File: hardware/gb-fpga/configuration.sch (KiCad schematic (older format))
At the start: 13 parts, among them U1 xc7s25ftgb196, U2 MX25R3235FZBxx1

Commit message: Switch from 0603 to 0402 footprints
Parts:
- C1: footprint Capacitor_SMD:C_0603_1608Metric -> Capacitor_SMD:C_0402_1005Metric
- D1: footprint LED_SMD:LED_0603_1608Metric -> LED_SMD:LED_0402_1005Metric
- R1, R2, R3, R4, R5, R6, R7, R8, R9: footprint Resistor_SMD:R_0603_1608Metric -> Resistor_SMD:R_0402_1005Metric
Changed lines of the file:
@@
 F 0 "C1" H 9692 3746 50  0000 L CNN
 F 1 "100nF" H 9692 3655 50  0000 L CNN
-F 2 "Capacitor_SMD:C_0603_1608Metric" H 9600 3700 50  0001 C CNN
+F 2 "Capacitor_SMD:C_0402_1005Metric" H 9600 3700 50  0001 C CNN
 F 3 "~" H 9600 3700 50  0001 C CNN
 	1    9600 3700
@@
 F 0 "R1" H 7400 3400 50  0000 C CNN
 F 1 "4.7k" H 7400 3500 50  0000 C CNN
-F 2 "Resistor_SMD:R_0603_1608Metric" H 7550 3450 50  0001 C CNN
+F 2 "Resistor_SMD:R_0402_1005Metric" H 7550 3450 50  0001 C CNN
 F 3 "~" H 7550 3450 50  0001 C CNN
 	1    7550 3450
@@
 F 0 "R3" H 7050 3400 50  0000 C CNN
 F 1 "1.8k" H 7050 3500 50  0000 C CNN
-F 2 "Resistor_SMD:R_0603_1608Metric" H 7200 3450 50  0001 C CNN
+F 2 "Resistor_SMD:R_0402_1005Metric" H 7200 3450 50  0001 C CNN
 F 3 "~" H 7200 3450 50  0001 C CNN
 	1    7200 3450
@@
 F 0 "R2" H 6700 3400 50  0000 C CNN
 F 1 "1.8k" H 6700 3500 50  0000 C CNN
-F 2 "Resistor_SMD:R_0603_1608Metric" H 6850 3450 50  0001 C CNN
+F 2 "Resistor_SMD:R_0402_1005Metric" H 6850 3450 50  0001 C CNN
 F 3 "~" H 6850 3450 50  0001 C CNN
 	1    6850 3450
@@
 F 0 "R7" H 2150 3150 50  0000 C CNN
 F 1 "4.7k" H 2150 3250 50  0000 C CNN
-F 2 "Resistor_SMD:R_0603_1608Metric" H 2300 3200 50  0001 C CNN
+F 2 "Resistor_SMD:R_0402_1005Metric" H 2300 3200 50  0001 C CNN
 F 3 "~" H 2300 3200 50  0001 C CNN
 	1    2300 3200
@@
 F 0 "R6" H 1850 3150 50  0000 C CNN
 F 1 "4.7k" H 1850 3250 50  0000 C CNN
-F 2 "Resistor_SMD:R_0603_1608Metric" H 2000 3200 50  0001 C CNN
+F 2 "Resistor_SMD:R_0402_1005Metric" H 2000 3200 50  0001 C CNN
 F 3 "~" H 2000 3200 50  0001 C CNN
 	1    2000 3200
@@
 F 0 "R5" H 1550 3150 50  0000 C CNN
 F 1 "4.7k" H 1550 3250 50  0000 C CNN
-F 2 "Resistor_SMD:R_0603_1608Metric" H 1700 3200 50  0001 C CNN
+F 2 "Resistor_SMD:R_0402_1005Metric" H 1700 3200 50  0001 C CNN
 F 3 "~" H 1700 3200 50  0001 C CNN
 	1    1700 3200
@@
 F 0 "R8" H 2650 3050 50  0000 C CNN
 F 1 "200" H 2650 3150 50  0000 C CNN
-F 2 "Resistor_SMD:R_0603_1608Metric" H 2800 3100 50  0001 C CNN
+F 2 "Resistor_SMD:R_0402_1005Metric" H 2800 3100 50  0001 C CNN
 F 3 "~" H 2800 3100 50  0001 C CNN
 	1    2800 3100
@@
 F 0 "D1" V 2196 4730 50  0000 R CNN
 F 1 "LED" V 2105 4730 50  0000 R CNN
-F 2 "LED_SMD:LED_0603_1608Metric" V 2150 4800 50  0001 C CNN
+F 2 "LED_SMD:LED_0402_1005Metric" V 2150 4800 50  0001 C CNN
 F 3 "~" V 2150 4800 50  0001 C CNN
 	1    2150 4800
@@
 F 0 "R9" H 2000 4400 50  0000 C CNN
 F 1 "100" H 2000 4500 50  0000 C CNN
-F 2 "Resistor_SMD:R_0603_1608Metric" H 2150 4450 50  0001 C CNN
+F 2 "Resistor_SMD:R_0402_1005Metric" H 2150 4450 50  0001 C CNN
 F 3 "~" H 2150 4450 50  0001 C CNN
 	1    2150 4450
@@
 F 0 "R4" H 5550 3050 50  0000 C CNN
 F 1 "1k" H 5550 3150 50  0000 C CNN
-F 2 "Resistor_SMD:R_0603_1608Metric" H 5700 3100 50  0001 C CNN
+F 2 "Resistor_SMD:R_0402_1005Metric" H 5700 3100 50  0001 C CNN
 F 3 "~" H 5700 3100 50  0001 C CNN
 	1    5700 3100

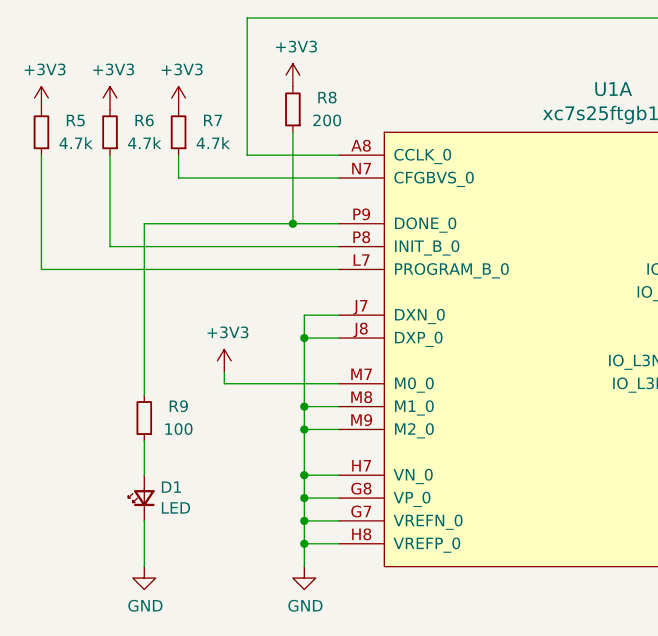
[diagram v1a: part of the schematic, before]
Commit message: Add chargeing indicator LED
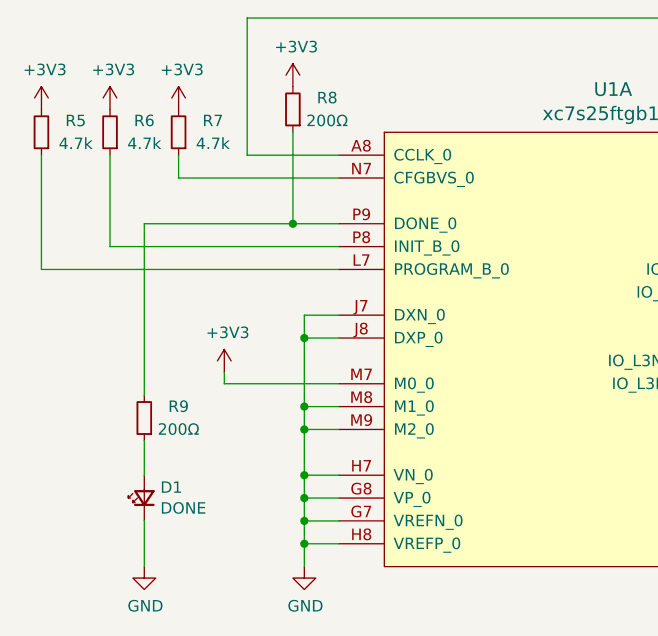
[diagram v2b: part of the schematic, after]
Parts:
- D1: value LED -> DONE
- R8: value 200 -> 200Ω
- R9: value 100 -> 200Ω
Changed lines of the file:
@@
 P 2800 3100
 F 0 "R8" H 2650 3050 50  0000 C CNN
-F 1 "200" H 2650 3150 50  0000 C CNN
+F 1 "200Ω" H 2650 3150 50  0000 C CNN
 F 2 "Resistor_SMD:R_0402_1005Metric" H 2800 3100 50  0001 C CNN
 F 3 "~" H 2800 3100 50  0001 C CNN
@@
 P 2150 4800
 F 0 "D1" V 2196 4730 50  0000 R CNN
-F 1 "LED" V 2105 4730 50  0000 R CNN
+F 1 "DONE" V 2105 4730 50  0000 R CNN
 F 2 "LED_SMD:LED_0402_1005Metric" V 2150 4800 50  0001 C CNN
 F 3 "~" V 2150 4800 50  0001 C CNN
@@
 P 2150 4450
 F 0 "R9" H 2000 4400 50  0000 C CNN
-F 1 "100" H 2000 4500 50  0000 C CNN
+F 1 "200Ω" H 2000 4500 50  0000 C CNN
 F 2 "Resistor_SMD:R_0402_1005Metric" H 2150 4450 50  0001 C CNN
 F 3 "~" H 2150 4450 50  0001 C CNN

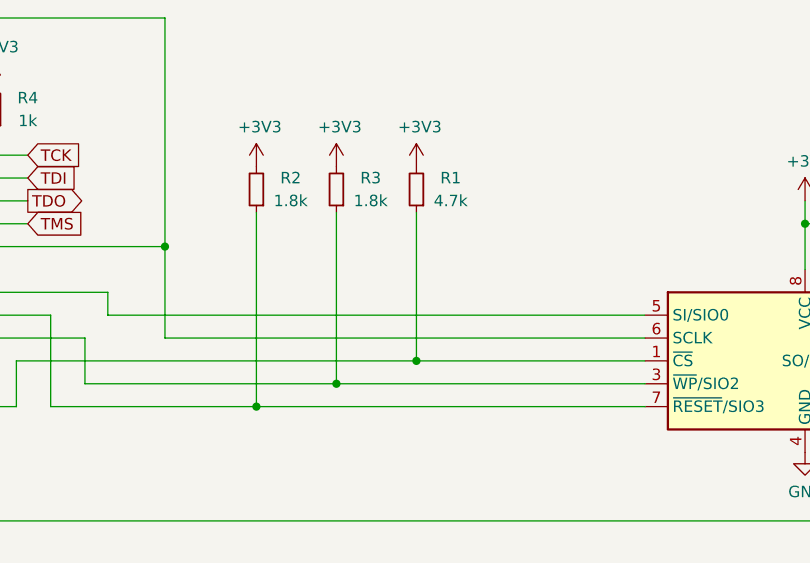
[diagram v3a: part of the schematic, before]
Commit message: Add test points and update gerber for pcb way
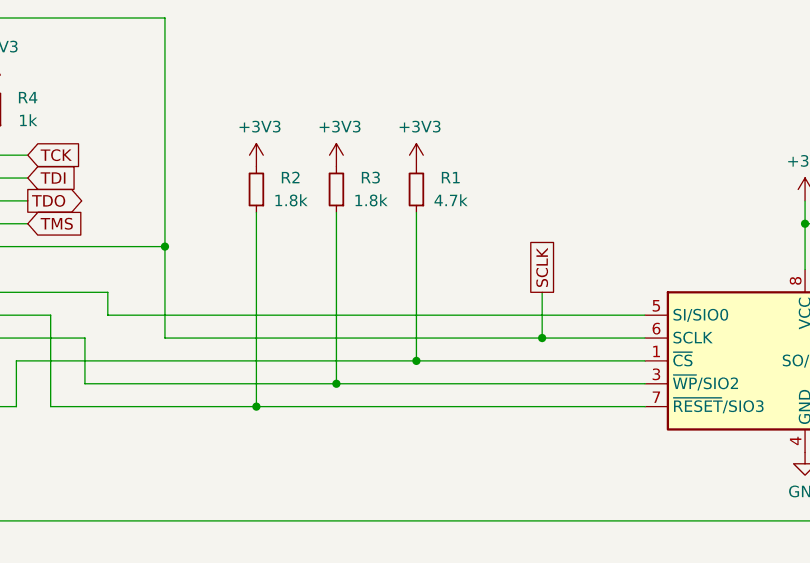
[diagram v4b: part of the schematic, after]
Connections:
- net SCLK: now reaches U1.A10 (IO_L3N_T0_DQS_EMCCLK_14), U1.A8 (CCLK_0), U2.6 (SCLK)
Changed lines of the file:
@@
 $Descr A4 11693 8268
 encoding utf-8
-Sheet 2 8
+Sheet 2 9
 Title "Configuration"
 Date ""
@@
 	7550 4200 7550 3550
 Wire Wire Line
-	8550 4100 6450 4100
+	8550 4100 8100 4100
 Wire Wire Line
 	6450 4100 6450 3700
@@
 Text GLabel 5850 3600 2    50   Input ~ 0
 TMS
+Text GLabel 8100 3900 1    50   UnSpc ~ 0
+SCLK
+Wire Wire Line
+	8100 3900 8100 4100
+Connection ~ 8100 4100
+Wire Wire Line
+	8100 4100 6450 4100
 $EndSCHEMATC

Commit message: Update bom
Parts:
- C1: Manufacturer Part Number (none) -> CL05B104KO5NNNC
- D1: Manufacturer Part Number (none) -> NCD0402G1
- R1, R5, R6, R7: Manufacturer Part Number (none) -> RC0402JR-074K7L
- R2, R3: Manufacturer Part Number (none) -> RC0402JR-071K8L
- R4: Manufacturer Part Number (none) -> RC0402JR-071KL
- R8, R9: Manufacturer Part Number (none) -> AC0402JR-07200RL
- U1: Manufacturer Part Number (none) -> XC7S25-1FTGB196C
- U2: Manufacturer Part Number (none) -> MX25R3235FZBIL0
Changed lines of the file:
@@
 F 2 "Capacitor_SMD:C_0402_1005Metric" H 9600 3700 50  0001 C CNN
 F 3 "~" H 9600 3700 50  0001 C CNN
+F 4 "CL05B104KO5NNNC" H 9600 3700 50  0001 C CNN "Manufacturer Part Number"
 	1    9600 3700
 	1    0    0    -1
@@
 F 2 "Resistor_SMD:R_0402_1005Metric" H 7550 3450 50  0001 C CNN
 F 3 "~" H 7550 3450 50  0001 C CNN
+F 4 "RC0402JR-074K7L" H 7550 3450 50  0001 C CNN "Manufacturer Part Number"
 	1    7550 3450
 	-1   0    0    1
@@
 F 2 "Package_SON:USON-8_4.0x3.0mm_P0.8mm" H 9050 3600 50  0001 C CNN
 F 3 "http://www.macronix.com/Lists/Datasheet/Attachments/7534/MX25R3235F,%20Wide%20Range,%2032Mb,%20v1.6.pdf" H 9050 4200 50  0001 C CNN
+F 4 "MX25R3235FZBIL0" H 9050 4200 50  0001 C CNN "Manufacturer Part Number"
 	1    9050 4200
 	1    0    0    -1
@@
 F 2 "Resistor_SMD:R_0402_1005Metric" H 7200 3450 50  0001 C CNN
 F 3 "~" H 7200 3450 50  0001 C CNN
+F 4 "RC0402JR-071K8L" H 7200 3450 50  0001 C CNN "Manufacturer Part Number"
 	1    7200 3450
 	-1   0    0    1
@@
 F 2 "Resistor_SMD:R_0402_1005Metric" H 6850 3450 50  0001 C CNN
 F 3 "~" H 6850 3450 50  0001 C CNN
+F 4 "RC0402JR-071K8L" H 6850 3450 50  0001 C CNN "Manufacturer Part Number"
 	1    6850 3450
 	-1   0    0    1
@@
 F 2 "Resistor_SMD:R_0402_1005Metric" H 2300 3200 50  0001 C CNN
 F 3 "~" H 2300 3200 50  0001 C CNN
+F 4 "RC0402JR-074K7L" H 2300 3200 50  0001 C CNN "Manufacturer Part Number"
 	1    2300 3200
 	-1   0    0    1
@@
 F 2 "Resistor_SMD:R_0402_1005Metric" H 2000 3200 50  0001 C CNN
 F 3 "~" H 2000 3200 50  0001 C CNN
+F 4 "RC0402JR-074K7L" H 2000 3200 50  0001 C CNN "Manufacturer Part Number"
 	1    2000 3200
 	-1   0    0    1
@@
 F 2 "Resistor_SMD:R_0402_1005Metric" H 1700 3200 50  0001 C CNN
 F 3 "~" H 1700 3200 50  0001 C CNN
+F 4 "RC0402JR-074K7L" H 1700 3200 50  0001 C CNN "Manufacturer Part Number"
 	1    1700 3200
 	-1   0    0    1
@@
 F 2 "" H 3200 3350 60  0001 L CNN
 F 3 "" H 3200 3150 60  0001 L CNN
+F 4 "XC7S25-1FTGB196C" H 3000 3300 50  0001 C CNN "Manufacturer Part Number"
 	1    3000 3300
 	1    0    0    -1
@@
 F 2 "Resistor_SMD:R_0402_1005Metric" H 2800 3100 50  0001 C CNN
 F 3 "~" H 2800 3100 50  0001 C CNN
+F 4 "AC0402JR-07200RL" H 2800 3100 50  0001 C CNN "Manufacturer Part Number"
 	1    2800 3100
 	-1   0    0    1
@@
 F 2 "LED_SMD:LED_0402_1005Metric" V 2150 4800 50  0001 C CNN
 F 3 "~" V 2150 4800 50  0001 C CNN
+F 4 "NCD0402G1" H 2150 4800 50  0001 C CNN "Manufacturer Part Number"
 	1    2150 4800
 	0    -1   -1   0
@@
 F 2 "Resistor_SMD:R_0402_1005Metric" H 2150 4450 50  0001 C CNN
 F 3 "~" H 2150 4450 50  0001 C CNN
+F 4 "AC0402JR-07200RL" H 2150 4450 50  0001 C CNN "Manufacturer Part Number"
 	1    2150 4450
 	-1   0    0    1
@@
 F 2 "Resistor_SMD:R_0402_1005Metric" H 5700 3100 50  0001 C CNN
 F 3 "~" H 5700 3100 50  0001 C CNN
+F 4 "RC0402JR-071KL" H 5700 3100 50  0001 C CNN "Manufacturer Part Number"
 	1    5700 3100
 	-1   0    0    1

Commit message: Update BOM with substitute for flash memory
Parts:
- U2: Manufacturer Part Number MX25R3235FZBIL0 -> MX25L3233FZBI-08Q
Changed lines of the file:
@@
 F 2 "Package_SON:USON-8_4.0x3.0mm_P0.8mm" H 9050 3600 50  0001 C CNN
 F 3 "http://www.macronix.com/Lists/Datasheet/Attachments/7534/MX25R3235F,%20Wide%20Range,%2032Mb,%20v1.6.pdf" H 9050 4200 50  0001 C CNN
-F 4 "MX25R3235FZBIL0" H 9050 4200 50  0001 C CNN "Manufacturer Part Number"
+F 4 "MX25L3233FZBI-08Q" H 9050 4200 50  0001 C CNN "Manufacturer Part Number"
 	1    9050 4200
 	1    0    0    -1
